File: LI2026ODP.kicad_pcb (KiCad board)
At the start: 4 copper layers, 18.8 x 39.9 mm, 34 parts, among them J1 9-1437539-2, J2 Conn_01x05_Male, U1 LM2936MM-3.3, U2 STM32G0B1KET6, U3 max6921aui

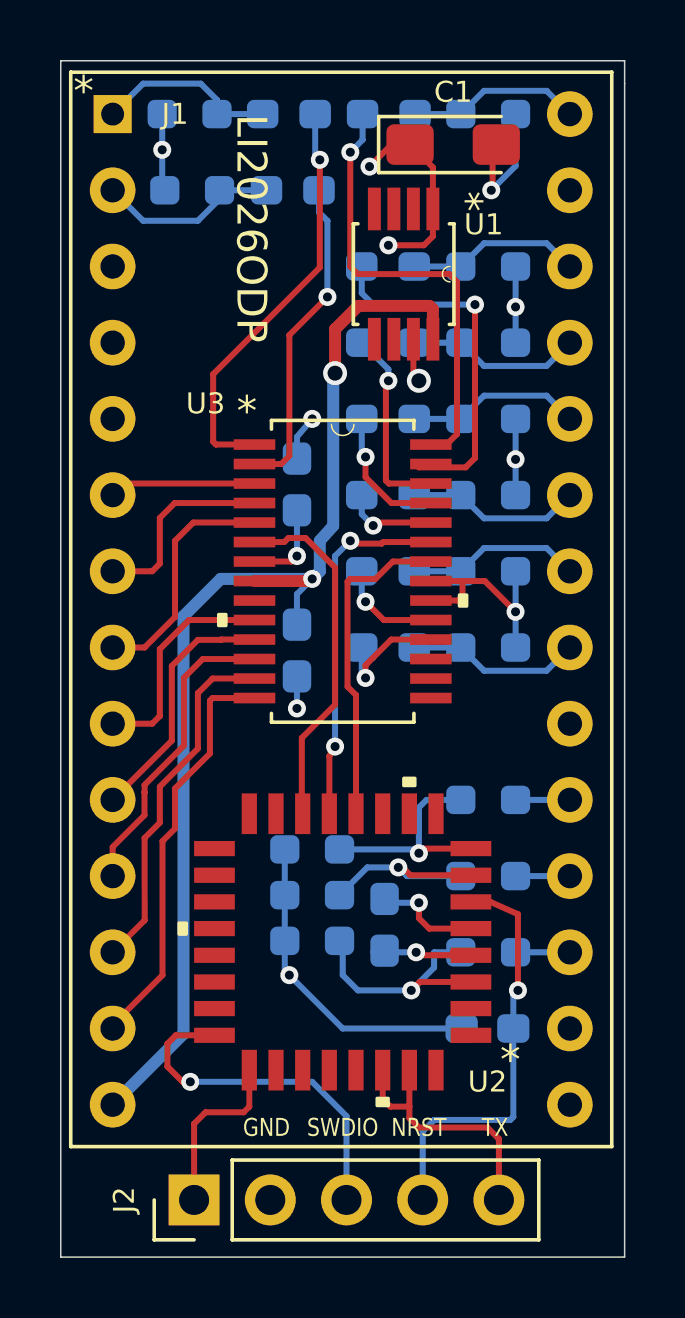
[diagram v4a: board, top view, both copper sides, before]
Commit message: Change BLANK control of MAX6921
from the hardwired to the software control.
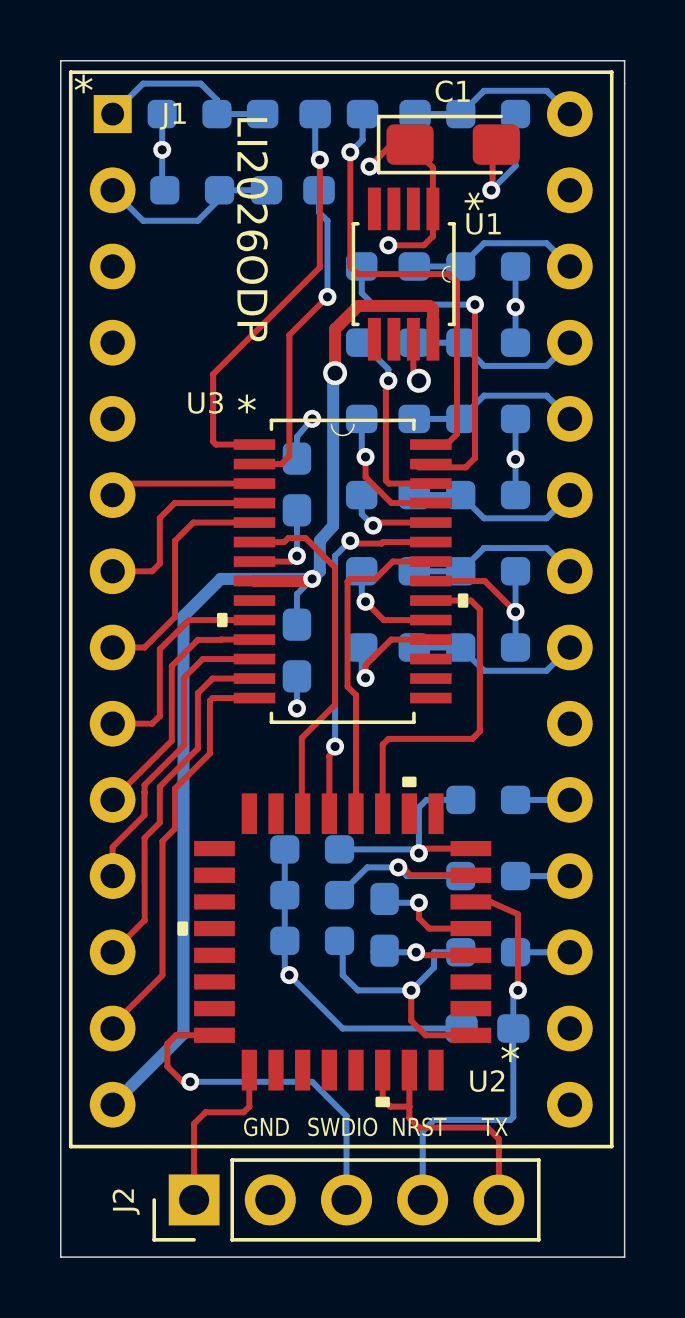
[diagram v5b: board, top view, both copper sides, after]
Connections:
- U2 pad 1: Net-(U2-Pad1) -> /RKEY1
- U2 pad 11: Net-(U2-Pad11) -> /BLANK
- U2 pad 3: /RKEY1 -> Net-(U2-Pad3)
- U3 pad 20: GND -> /BLANK
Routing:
- net /BLANK: track 0.00 -> 11.5 mm
- net GND: track 38.2 -> 36.6 mm
- net /RKEY1: track 8.11 -> 9.21 mm
